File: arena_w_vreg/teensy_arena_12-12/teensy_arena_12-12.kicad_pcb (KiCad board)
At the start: 4 copper layers, 254 x 254 mm, 87 parts, among them J1 Barrel_Jack, J2 Conn_01x04, J3 Conn_01x04, P1 CONN15, P10 CONN15, P11 CONN15, P12 CONN15, P2 CONN15, P3 CONN15, P4 CONN15, P5 CONN15, P6 CONN15, P7 CONN15, P8 CONN15, P9 CONN15, Q2 MOSFET_NCHAN, SW1 SW_SPDT, U1 TXB0108PW, U10 AZ1084-5.0, U11 AZ1084-5.0, U12 AZ1084-5.0, U13 AZ1084-5.0, U14 AZ1084-5.0, U15 AZ1084-5.0, U16 AZ1084-5.0, U17 AZ1084-5.0, U18 Teensy4.1, U2 TXB0108PW, U3 TXB0108PW, U4 TXB0108PW, U5 TXB0108PW, U6 AZ1084-5.0, U7 AZ1084-5.0, U8 AZ1084-5.0, U9 AZ1084-5.0

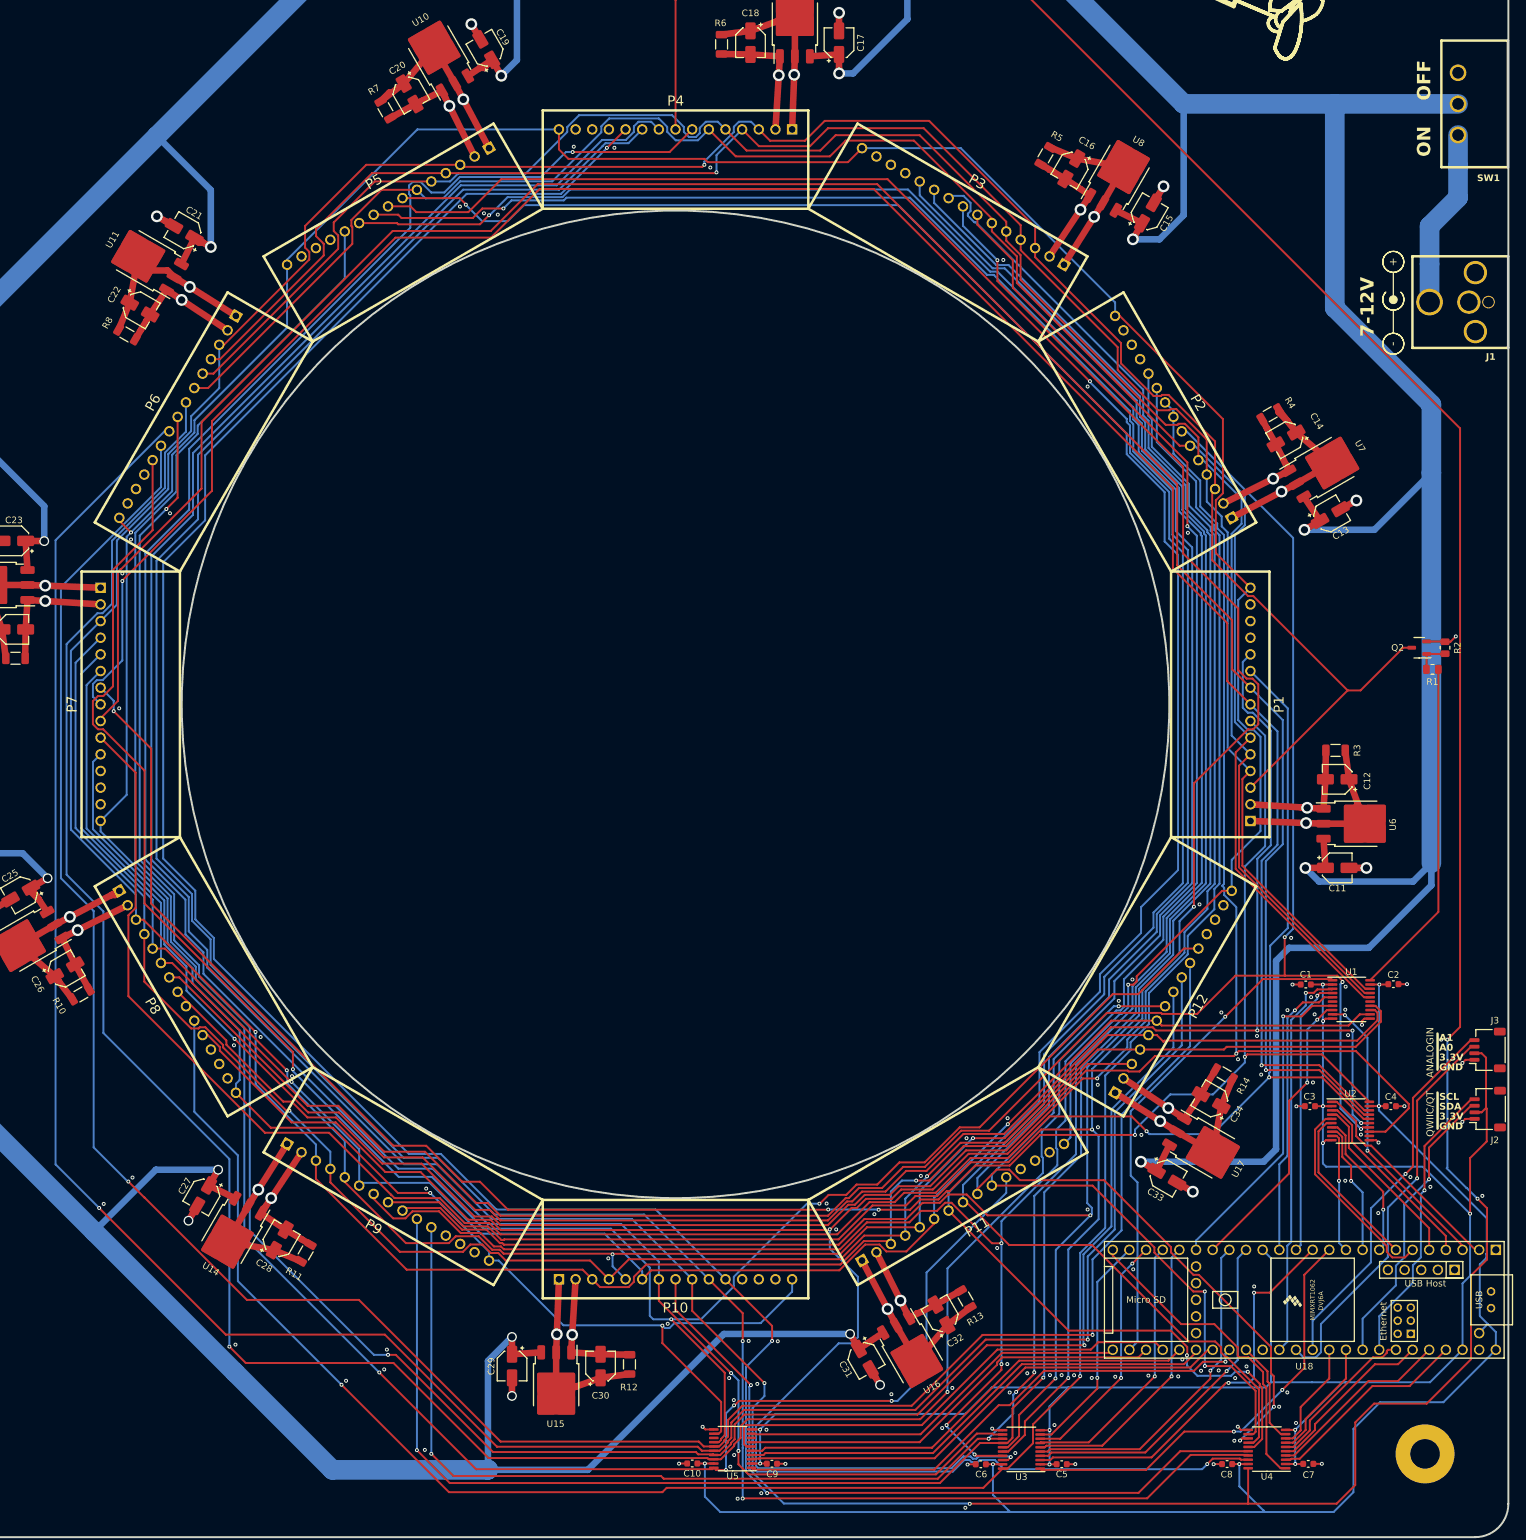
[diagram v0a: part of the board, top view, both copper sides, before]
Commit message: Fixed outstanding layout violations 12-12 teensy controller/arena.
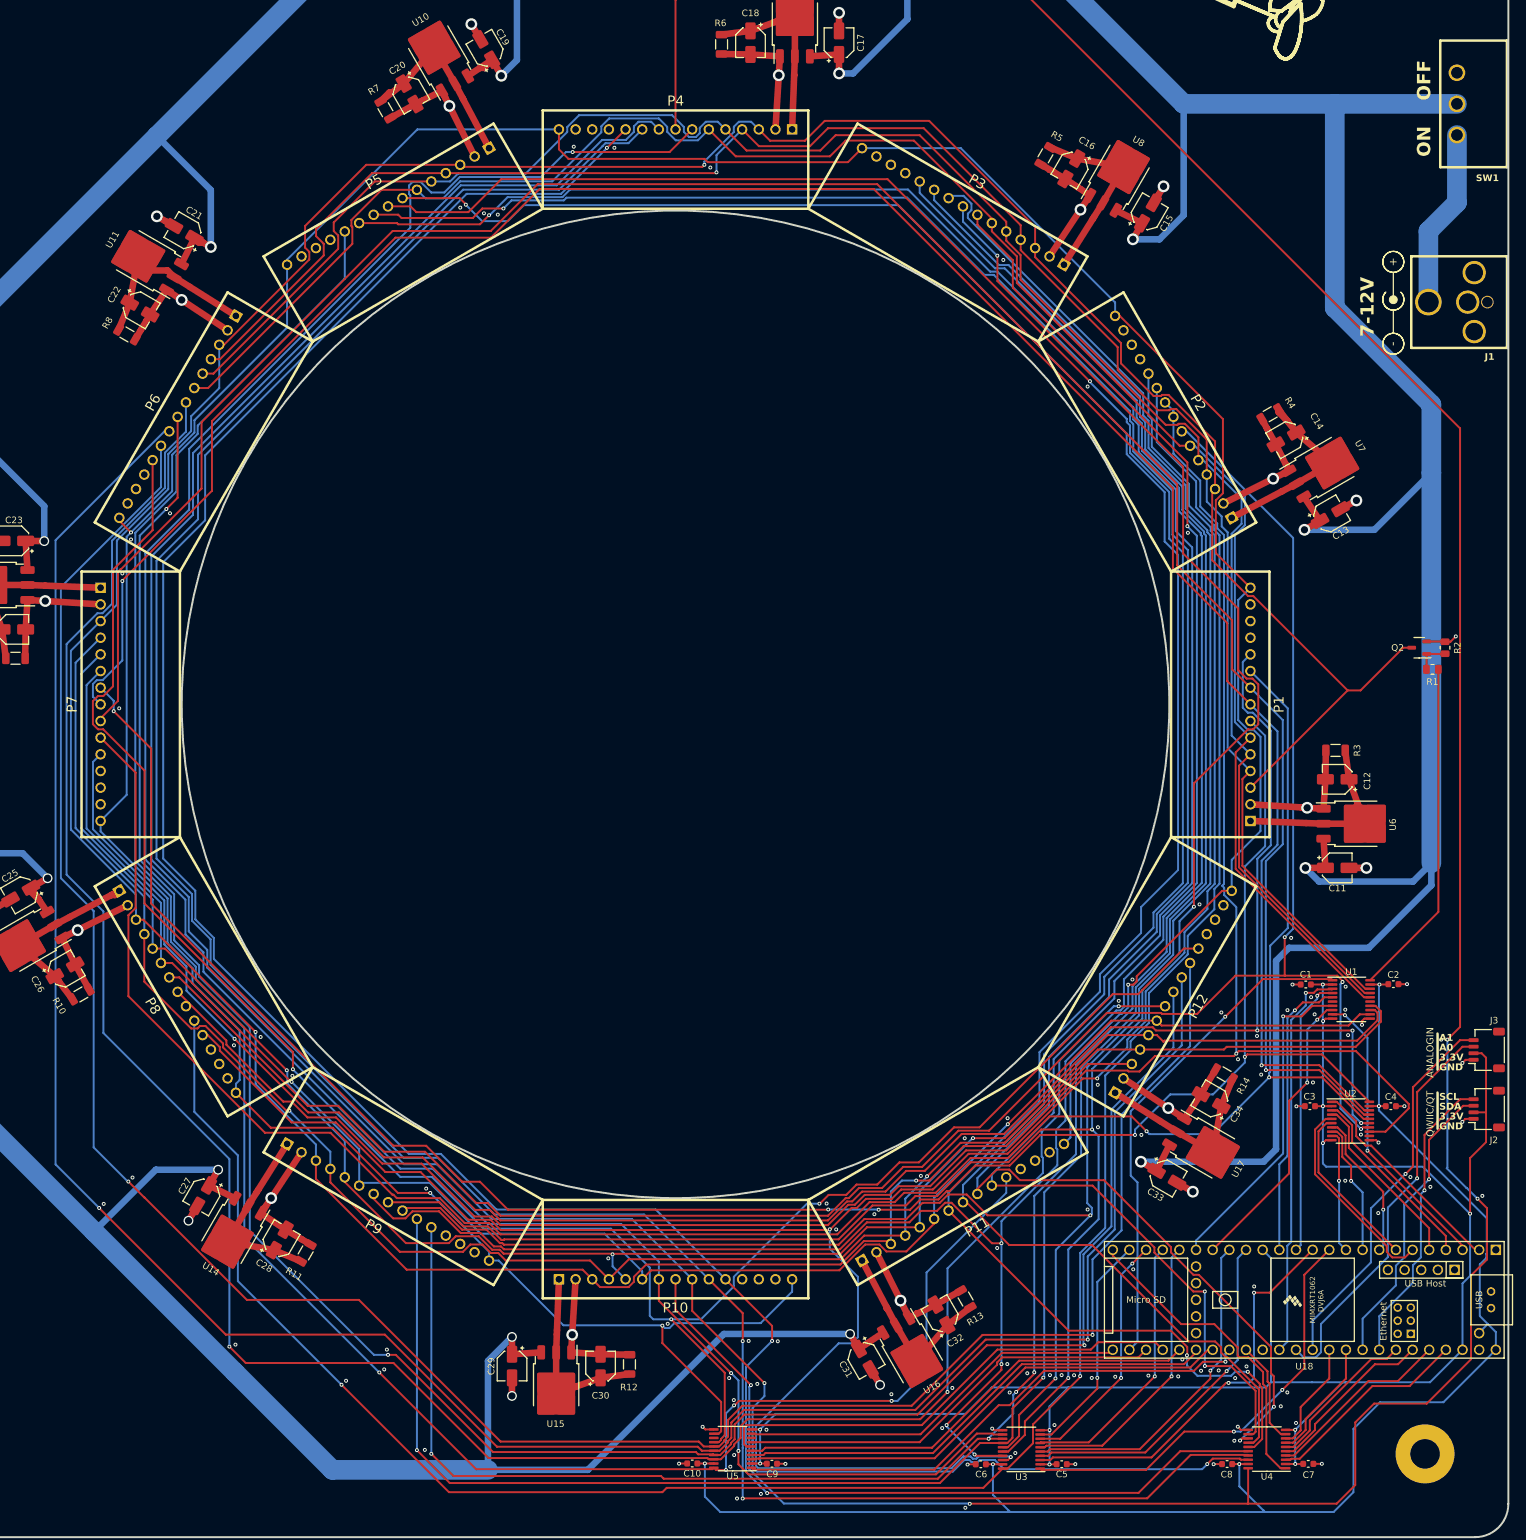
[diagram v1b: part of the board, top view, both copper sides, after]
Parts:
- moved J1 0.17 mm to (304.6, 116.5)
- moved SW1 0.17 mm to (299.5, 86.2)
- moved J2 0.15 mm to (301.5, 239.5)
- moved J3 0.12 mm to (301.5, 230.5)
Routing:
- net Net-(SW1-A): track 37.8 -> 27.3 mm
- net /Teensy/A1: track 57.8 -> 59.2 mm
- net /Teensy/SCL: track 44.5 -> 45.4 mm
- net /Teensy/A0: track 61.2 -> 61.8 mm
- net /Teensy/SDA: track 44.6 -> 45.2 mm
- net GND: track 343.1 -> 343.0 mm, vias 137 -> 138
- net /Panel Headers/POW.5V_HDR_9: vias 1 -> 0
- net /Panel Headers/POW.5V_HDR_8: vias 1 -> 0
- net /Panel Headers/POW.5V_HDR_7: vias 1 -> 0
- net /Panel Headers/POW.5V_HDR_6: vias 1 -> 0
- net /Panel Headers/POW.5V_HDR_5: vias 1 -> 0
- net /Panel Headers/POW.5V_HDR_4: vias 1 -> 0
- net /Panel Headers/POW.5V_HDR_3: vias 1 -> 0
- net /Panel Headers/POW.5V_HDR_2: vias 1 -> 0
- net /Panel Headers/POW.5V_HDR_12: vias 1 -> 0
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
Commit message: Completed initial version of fab files.
Note, there is an issue with the placement of the voltage regulators
which needs to be resolved. Discrepancy between kicad and JLCPCB.
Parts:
- C19: value 10F -> 10uF
- R10, R11, R12, R13, R14, R3, R4, R5, R6, R7, R8, R9: footprint Capacitor_SMD:C_1206_3216Metric -> Resistor_SMD:R_1206_3216Metric
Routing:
- net /Panel Headers/POW.5V_HDR_8: track 39.3 -> 37.8 mm
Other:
- board text added: "ANALOG IN"
- board text removed: "ANALOGIN"
